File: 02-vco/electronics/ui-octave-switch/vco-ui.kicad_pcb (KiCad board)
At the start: 2 copper layers, 58 x 110 mm, 40 parts, among them J1 Conn_01x04, J2 Conn_02x05_Odd_Even, J3 Conn_02x03_Odd_Even, J4 Conn_01x02, J5 Conn_02x02_Counter_Clockwise, J6 Conn_01x06, U1 0203

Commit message: Designed v0.2 VCO UI (with octave switch)
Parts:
- removed the G*** at (169.3, 149.5)
- removed the G*** at (146.5, 129.6)
- removed the G*** at (163.6, 126.2)
- removed the G*** at (169.0, 63.4)
- removed the G*** at (173.5, 55.2)
- removed JP2, JP3: Jumper_2_Open, Connector_PinHeader_2.54mm:PinHeader_1x02_P2.54mm_Horizontal
- removed RV_FINE1, RV_TUNE1: 100k, Shmoergh_Custom_Footprints:Potentiometer_Bourns_Single-PTV09A
- added C1: C, Capacitor_THT:C_Disc_D5.0mm_W2.5mm_P2.50mm, F.Cu at (162.6, 46.0)
- added C2: C, Capacitor_THT:C_Disc_D5.0mm_W2.5mm_P2.50mm, F.Cu at (179.4, 53.7)
- added G***: LOGO, Shmoergh_Logo:Gyeszno, F.Cu at (177.5, 74.1)
- added G***: LOGO, Shmoergh_Logo:Gyeszno, B.Cu at (159.6, 103.3)
- added G***: LOGO, Shmoergh_Logo:Gyeszno, B.Cu at (144.6, 133.5)
- added R10: 2k, Shmoergh_Custom_Footprints:R_Axial_DIN0207_L6.3mm_D2.5mm_P7.62mm_Horizontal, F.Cu at (160.1, 56.7)
- added R11: 10k (0.1%), Shmoergh_Custom_Footprints:R_Axial_DIN0207_L6.3mm_D2.5mm_P7.62mm_Horizontal, F.Cu at (148.6, 67.0)
- added R12: 10k (0.1%), Shmoergh_Custom_Footprints:R_Axial_DIN0207_L6.3mm_D2.5mm_P7.62mm_Horizontal, F.Cu at (151.8, 74.6)
- added R13: 10k (0.1%), Shmoergh_Custom_Footprints:R_Axial_DIN0207_L6.3mm_D2.5mm_P7.62mm_Horizontal, F.Cu at (155.0, 74.6)
- added R14: 10k (0.1%), Shmoergh_Custom_Footprints:R_Axial_DIN0207_L6.3mm_D2.5mm_P7.62mm_Horizontal, F.Cu at (158.2, 74.6)
- added R15: 10k (0.1%), Shmoergh_Custom_Footprints:R_Axial_DIN0207_L6.3mm_D2.5mm_P7.62mm_Horizontal, F.Cu at (161.3, 74.6)
- added R9: 220k, Shmoergh_Custom_Footprints:R_Axial_DIN0207_L6.3mm_D2.5mm_P7.62mm_Horizontal, F.Cu at (175.7, 119.9)
- added RV_FINE_TUNE1: 100k, Shmoergh_Custom_Footprints:Potentiometer_Bourns_Single-PTV09A, F.Cu at (153.0, 83.0)
- added RV_MAIN_VCO_5V1: 10k, Potentiometer_THT:Potentiometer_Bourns_3006P_Horizontal, F.Cu at (153.8, 62.2)
- added TP_5V1: TP 5V, TestPoint:TestPoint_THTPad_2.0x2.0mm_Drill1.0mm, F.Cu at (145.2, 67.0)
- added U2: TL072, Package_DIP:DIP-8_W7.62mm_LongPads, F.Cu at (165.9, 53.7)
- added U3: 0203, Shmoergh_Custom_Footprints:SR1712-0203, F.Cu at (141.0, 55.0)
- added U_5VREF1: LM336Z5, Package_TO_SOT_THT:TO-92L_Inline_Wide, F.Cu at (159.8, 48.8)
- R1: value 130k -> 100k
- R2, R3: value 100k -> 10k-1M
- R4, R5: value 510k -> 100k
- R7: value 220k -> 100k
- U1: value 0203 -> 0204; footprint Shmoergh_Custom_Footprints:SR1712-0203 -> Shmoergh_Custom_Footprints:SR1712-0204
- moved G*** 76.1 mm to (130.0, 125.8)
- moved J4 72.7 mm to (126.7, 53.2)
- moved G*** 61.9 mm to (168.6, 70.3), turned to 0 degrees
- moved R3 52.8 mm to (178.6, 56.8), turned to -90 degrees
- moved R2 43.3 mm to (175.4, 56.8), turned to -90 degrees
- moved R6 40.8 mm to (169.1, 56.8), turned to -90 degrees
- moved R5 32.1 mm to (172.3, 64.4), turned to 90 degrees
- moved R8 30.2 mm to (175.7, 102.2), turned to -90 degrees
- moved R4 29.7 mm to (128.1, 95.7), turned to 0 degrees
- moved U1 28.3 mm to (137.0, 83.0), turned to 0 degrees
- moved G*** 23.8 mm to (137.0, 83.0)
- moved R7 19.9 mm to (165.9, 56.8), turned to -90 degrees
- moved R1 11.4 mm to (130.1, 111.1), turned to 90 degrees
- moved JP1 0.26 mm to (170.9, 123.8)
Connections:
- JP1 pad 1: NOISE -> SUB
- JP1 pad 3: SUB -> NOISE
- R1 pad 1: +12V -> Net-(J_CV1-PadT)
- R1 pad 2: Net-(R1-Pad2) -> CV
- R2 pad 1: Net-(R2-Pad1) -> Net-(U2A-+)
- R2 pad 2: CV -> PREC_1V
- R3 pad 1: Net-(J_CV1-PadT) -> GND
- R3 pad 2: CV -> Net-(U2A-+)
- R4 pad 1: +12V -> CV
- R5 pad 1: Net-(R5-Pad1) -> PREC_1V
- R5 pad 2: -12V -> Net-(U2A--)
- R6 pad 1: Net-(R6-Pad1) -> Net-(U2A--)
- R6 pad 2: CV -> Net-(R6-Pad2)
- R7 pad 1: Net-(R7-Pad1) -> Net-(R6-Pad2)
- R7 pad 2: SQR_SHAPE -> CV
- R8 pad 1: Net-(J_PWM1-PadT) -> Net-(R8-Pad1)
- RV_PWM1 pad 2: Net-(R7-Pad1) -> Net-(R8-Pad1)
- U1 pad 1: Net-(J_OUT1-PadT) -> Net-(R4-Pad2)
- U1 pad 2: TRI -> GND
- U1 pad 3: SAW -> PREC_1V
- U1 pad 4: SQR -> PREC_2V
- U1 pad 5: unconnected-(U1-Pad5) -> PREC_3V
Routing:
- net -12V: track 24.2 -> 102.5 mm
- net PREC_1V: track 0.00 -> 73.9 mm, vias 0 -> 2
- net Net-(U2A-+): track 0.00 -> 64.1 mm, vias 0 -> 2
- net TRI: track 126.0 -> 69.0 mm
- net Net-(J_PWM1-PadT): track 52.7 -> 6.70 mm
- net CV: track 39.7 -> 85.4 mm, vias 0 -> 4
- net PREC_2V: track 0.00 -> 44.2 mm
- net SAW: track 126.0 -> 170.1 mm, vias 0 -> 2
- net +5V: track 0.00 -> 43.8 mm
- net PREC_3V: track 0.00 -> 42.7 mm
- net Net-(J_CV1-PadT): track 78.5 -> 37.4 mm
- net Net-(R8-Pad1): track 0.00 -> 37.6 mm
- net SYNC_DEFAULT: track 46.3 -> 82.8 mm
- net Net-(R6-Pad1): track 35.2 -> 0.00 mm, vias 2 -> 0
- net Net-(R1-Pad2): track 30.9 -> 0.00 mm, vias 2 -> 0
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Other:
- board text added: "+5V"
- board text added: "HM-02 VCO UI V0.2 2025 SEPT"
- board text added: "OCTAVE"
- board text removed: "CV DEFAULT TO GROUND"
- board text removed: "FM DEFAULT TO GROUND"
- board text removed: "HM-02 VCO UI V0.1 2025 JULY"
- board text removed: "TUNE"

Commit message: Added VCO output to default connector
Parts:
- J6: value Conn_01x06 -> Conn_01x07; footprint Connector_PinSocket_2.54mm:PinSocket_1x06_P2.54mm_Vertical -> Connector_PinSocket_2.54mm:PinSocket_1x07_P2.54mm_Vertical
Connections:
- J6 pad 6: OUT_DEFAULT -> OUT_OUT
- J_OUT1 pad T: Net-(J_OUT1-PadT) -> OUT_OUT
- U3 pad 1: Net-(J_OUT1-PadT) -> OUT_OUT
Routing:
- net OUT_OUT: track 0.00 -> 149.6 mm
- net Net-(J_OUT1-PadT): track 147.0 -> 0.00 mm
- net OUT_DEFAULT: track 38.3 -> 36.0 mm
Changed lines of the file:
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@@
 	(net 19 "EXTRA_DEFAULT")
 	(net 20 "OUT_DEFAULT")
-	(net 21 "Net-(J_OUT1-PadT)")
+	(net 21 "OUT_OUT")
 	(net 22 "Net-(J_PWM1-PadT)")
 	(net 23 "Net-(R4-Pad2)")
@@
 			(layers "*.Cu" "*.Mask")
 			(remove_unused_layers no)
-			(net 21 "Net-(J_OUT1-PadT)")
+			(net 21 "OUT_OUT")
 			(pintype "bidirectional")
 		)
@@
 			(layers "*.Cu" "*.Mask")
 			(remove_unused_layers no)
-			(net 21 "Net-(J_OUT1-PadT)")
+			(net 21 "OUT_OUT")
 			(pinfunction "1")
 			(pintype "output")
@@
 		)
 	)
-	(footprint "Connector_PinSocket_2.54mm:PinSocket_1x06_P2.54mm_Vertical"
+	(footprint "Connector_PinSocket_2.54mm:PinSocket_1x07_P2.54mm_Vertical"
 		(locked yes)
 		(layer "B.Cu")
 		(at 132.5 151 -90)
-		(descr "Through hole straight socket strip, 1x06, 2.54mm pitch, single row (from Kicad 4.0.7), script generated")
-		(tags "Through hole socket strip THT 1x06 2.54mm single row")
+		(descr "Through hole straight socket strip, 1x07, 2.54mm pitch, single row (from Kicad 4.0.7), script generated")
+		(tags "Through hole socket strip THT 1x07 2.54mm single row")
 		(property "Reference" "J6"
-			(at -1.966 -15.122 0)
-			(layer "B.SilkS")
+			(at 0 2.77 90)
+			(layer "User.1")
 			(effects
 				(font
@@
 			)
 		)
-		(property "Value" "Conn_01x06"
-			(at 0 -15.47 90)
+		(property "Value" "Conn_01x07"
+			(at 0 -18.01 90)
 			(layer "B.Fab")
 			(effects
@@
 			)
 		)
-		(property "Description" "Generic connector, single row, 01x06, script generated (kicad-library-utils/schlib/autogen/connector/)"
+		(property "Description" "Generic connector, single row, 01x07, script generated (kicad-library-utils/schlib/autogen/connector/)"
 			(at 0 0 90)
 			(layer "B.Fab")
@@
 		)
 		(property "Part URL" "https://mou.sr/4lnf48h"
-			(at 0 0 90)
+			(at 0 0 270)
 			(unlocked yes)
 			(layer "B.Fab")
@@
 		)
 		(property "Vendor" "Mouser"
-			(at 0 0 90)
+			(at 0 0 270)
 			(unlocked yes)
 			(layer "B.Fab")
@@
 		)
 		(property "LCSC" ""
-			(at 0 0 90)
+			(at 0 0 270)
 			(unlocked yes)
 			(layer "B.Fab")
@@
 			)
 		)
+		(property "Part No." ""
+			(at 0 0 270)
+			(unlocked yes)
+			(layer "B.Fab")
+			(hide yes)
+			(effects
+				(font
+					(size 1 1)
+					(thickness 0.15)
+				)
+				(justify mirror)
+			)
+		)
 		(property ki_fp_filters "Connector*:*_1x??_*")
 		(sheetname "/")
@@
 		(fp_line
 			(start -1.33 -1.27)
-			(end -1.33 -14.03)
+			(end -1.33 -16.57)
 			(stroke
 				(width 0.12)
@@
 		(fp_line
 			(start 1.33 -1.27)
-			(end 1.33 -14.03)
+			(end 1.33 -16.57)
 			(stroke
 				(width 0.12)
@@
 		)
 		(fp_line
-			(start -1.33 -14.03)
-			(end 1.33 -14.03)
+			(start -1.33 -16.57)
+			(end 1.33 -16.57)
 			(stroke
 				(width 0.12)
@@
 		(fp_line
 			(start 1.75 1.8)
-			(end 1.75 -14.45)
+			(end 1.75 -17)
 			(stroke
 				(width 0.05)
@@
 		)
 		(fp_line
-			(start -1.8 -14.45)
+			(start -1.8 -17)
 			(end -1.8 1.8)
 			(stroke
@@
 		)
 		(fp_line
-			(start 1.75 -14.45)
-			(end -1.8 -14.45)
+			(start 1.75 -17)
+			(end -1.8 -17)
 			(stroke
 				(width 0.05)
@@
 		(fp_line
 			(start 1.27 0.635)
-			(end 1.27 -13.97)
+			(end 1.27 -16.51)
 			(stroke
 				(width 0.1)
@@
 		)
 		(fp_line
-			(start -1.27 -13.97)
+			(start -1.27 -16.51)
 			(end -1.27 1.27)
 			(stroke
@@
 		)
 		(fp_line
-			(start 1.27 -13.97)
-			(end -1.27 -13.97)
+			(start 1.27 -16.51)
+			(end -1.27 -16.51)
 			(stroke
 				(width 0.1)
@@
 		)
 		(fp_text user "${REFERENCE}"
-			(at 0 -6.35 180)
+			(at 0 -7.62 0)
 			(layer "B.Fab")
 			(effects
@@
 			(layers "*.Cu" "*.Mask")
 			(remove_unused_layers no)
-			(net 20 "OUT_DEFAULT")
+			(net 21 "OUT_OUT")
 			(pinfunction "Pin_6")
 			(pintype "passive")
 		)
+		(pad "7" thru_hole circle
+			(at 0 -15.24 270)
+			(size 1.7 1.7)
+			(drill 1)
+			(layers "*.Cu" "*.Mask")
+			(remove_unused_layers no)
+			(net 20 "OUT_DEFAULT")
+			(pinfunction "Pin_7")
+			(pintype "passive")
+		)
 		(embedded_fonts no)
-		(model "${KICAD9_3DMODEL_DIR}/Connector_PinSocket_2.54mm.3dshapes/PinSocket_1x06_P2.54mm_Vertical.step"
+		(model "${KICAD9_3DMODEL_DIR}/Connector_PinSocket_2.54mm.3dshapes/PinSocket_1x07_P2.54mm_Vertical.step"
 			(offset
 				(xyz 0 0 0)
@@
 		)
 	)
+	(gr_text "OUT"
+		(at 147.876 149.029 0)
+		(layer "F.SilkS")
+		(effects
+			(font
+				(size 1 0.75)
+				(thickness 0.17)
+				(bold yes)
+			)
+			(justify bottom)
+		)
+	)
 	(gr_text "NOISE"
 		(at 181.023 136.964 90)
@@
 	(segment
 		(start 162.862 150.553)
-		(end 161.211 152.204)
+		(end 160.957 152.458)
 		(width 0.508)
 		(layer "F.Cu")
@@
 	)
 	(segment
-		(start 161.211 152.204)
-		(end 146.404 152.204)
+		(start 160.957 152.458)
+		(end 149.198 152.458)
 		(width 0.508)
 		(layer "F.Cu")
@@
 	)
 	(segment
-		(start 146.404 152.204)
-		(end 145.2 151)
+		(start 149.198 152.458)
+		(end 147.74 151)
 		(width 0.508)
 		(layer "F.Cu")
@@
 	)
 	(segment
-		(start 125.143 141.155)
-		(end 130.731 146.743)
+		(start 125.143 61.272)
+		(end 125.143 141.155)
 		(width 0.508)
 		(layer "F.Cu")
@@
 	)
 	(segment
-		(start 130.731 152.077)
-		(end 131.747 153.093)
+		(start 166.672 153.347)
+		(end 169 151.019)
 		(width 0.508)
 		(layer "F.Cu")
@@
 	)
 	(segment
-		(start 131.85 60)
-		(end 126.415 60)
+		(start 147.749 153.347)
+		(end 166.672 153.347)
 		(width 0.508)
 		(layer "F.Cu")
@@
 	)
 	(segment
+		(start 145.2 153.338)
+		(end 145.209 153.347)
+		(width 0.508)
+		(layer "F.Cu")
+		(net 21)
+	)
+	(segment
+		(start 145.209 153.347)
+		(end 147.749 153.347)
+		(width 0.508)
+		(layer "F.Cu")
+		(net 21)
+	)
+	(segment
 		(start 130.731 146.743)
 		(end 130.731 152.077)
@@
 	)
 	(segment
-		(start 125.143 61.272)
-		(end 125.143 141.155)
+		(start 130.731 152.077)
+		(end 132.001 153.347)
 		(width 0.508)
 		(layer "F.Cu")
@@
 	)
 	(segment
-		(start 131.747 153.093)
-		(end 166.926 153.093)
+		(start 132.001 153.347)
+		(end 145.209 153.347)
 		(width 0.508)
 		(layer "F.Cu")
@@
 	)
 	(segment
-		(start 166.926 153.093)
-		(end 169 151.019)
+		(start 131.85 60)
+		(end 126.415 60)
+		(width 0.508)
+		(layer "F.Cu")
+		(net 21)
+	)
+	(segment
+		(start 125.143 141.155)
+		(end 130.731 146.743)
 		(width 0.508)
 		(layer "F.Cu")
@@
 		(width 0.508)
 		(layer "F.Cu")
+		(net 21)
+	)
+	(segment
+		(start 145.2 151)
+		(end 145.2 153.338)
+		(width 0.508)
+		(layer "F.Cu")

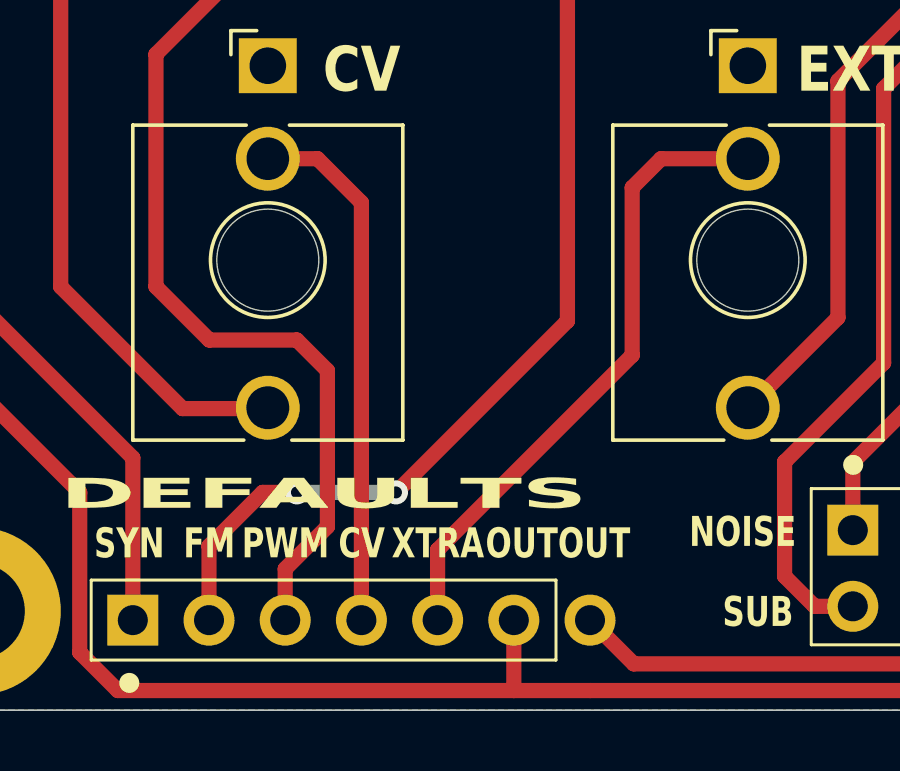
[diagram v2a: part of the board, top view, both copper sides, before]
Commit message: Added CV output to VCO default patch
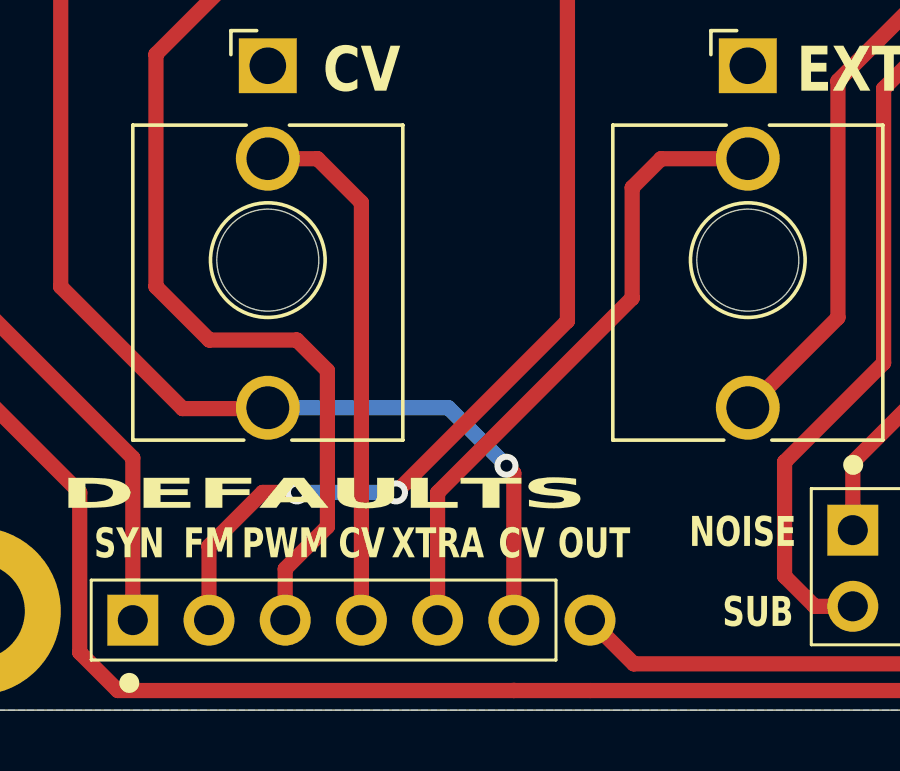
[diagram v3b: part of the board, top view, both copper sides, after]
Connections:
- J6 pad 6: OUT_OUT -> CV_INPUT
- J_CV1 pad T: Net-(J_CV1-PadT) -> CV_INPUT
- J_OUT1 pad T: OUT_OUT -> Net-(J_OUT1-PadT)
- R1 pad 1: Net-(J_CV1-PadT) -> CV_INPUT
- U3 pad 1: OUT_OUT -> Net-(J_OUT1-PadT)
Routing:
- net OUT_OUT: track 149.6 -> 0.00 mm
- net Net-(J_OUT1-PadT): track 0.00 -> 147.2 mm
- net CV_INPUT: track 0.00 -> 51.4 mm, vias 0 -> 1
- net Net-(J_CV1-PadT): track 37.4 -> 0.00 mm
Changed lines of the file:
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@@
 	(net 16 "SUB")
 	(net 17 "Net-(JP1-C)")
-	(net 18 "Net-(J_CV1-PadT)")
+	(net 18 "CV_INPUT")
 	(net 19 "EXTRA_DEFAULT")
 	(net 20 "OUT_DEFAULT")
-	(net 21 "OUT_OUT")
+	(net 21 "Net-(J_OUT1-PadT)")
 	(net 22 "Net-(J_PWM1-PadT)")
 	(net 23 "Net-(R4-Pad2)")
@@
 			(layers "*.Cu" "*.Mask")
 			(remove_unused_layers no)
-			(net 21 "OUT_OUT")
+			(net 21 "Net-(J_OUT1-PadT)")
 			(pintype "bidirectional")
 		)
@@
 			(layers "*.Cu" "*.Mask")
 			(remove_unused_layers no)
-			(net 18 "Net-(J_CV1-PadT)")
+			(net 18 "CV_INPUT")
 			(pintype "bidirectional")
 		)
@@
 			(layers "*.Cu" "*.Mask")
 			(remove_unused_layers no)
-			(net 18 "Net-(J_CV1-PadT)")
+			(net 18 "CV_INPUT")
 			(pintype "passive")
 		)
@@
 			(layers "*.Cu" "*.Mask")
 			(remove_unused_layers no)
-			(net 21 "OUT_OUT")
+			(net 21 "Net-(J_OUT1-PadT)")
 			(pinfunction "1")
 			(pintype "output")
@@
 			(layers "*.Cu" "*.Mask")
 			(remove_unused_layers no)
-			(net 21 "OUT_OUT")
+			(net 18 "CV_INPUT")
 			(pinfunction "Pin_6")
 			(pintype "passive")
@@
 		)
 	)
-	(gr_text "OUT"
+	(gr_text "CV"
 		(at 145.463 149.029 0)
 		(layer "F.SilkS" knockout)
@@
 	)
 	(segment
+		(start 145.2 151)
+		(end 145.2 146.099)
+		(width 0.508)
+		(layer "F.Cu")
+		(net 18)
+	)
+	(segment
+		(start 145.2 146.099)
+		(end 144.955 145.854)
+		(width 0.508)
+		(layer "F.Cu")
+		(net 18)
+	)
+	(segment
 		(start 130.096 111.056)
 		(end 130.096 139.885)
@@
 		(net 18)
 	)
+	(via
+		(at 144.955 145.854)
+		(size 0.8)
+		(drill 0.4)
+		(layers "F.Cu" "B.Cu")
+		(net 18)
+	)
 	(segment
-		(start 149.146 142.171)
-		(end 149.146 136.583)
+		(start 144.955 145.854)
+		(end 143.021 143.92)
 		(width 0.508)
-		(layer "F.Cu")
-		(net 19)
+		(layer "B.Cu")
+		(net 18)
+	)
+	(segment
+		(start 143.021 143.92)
+		(end 137 143.92)
+		(width 0.508)
+		(layer "B.Cu")
+		(net 18)
 	)
 	(segment
@@
 	)
 	(segment
-		(start 142.66 148.657)
-		(end 149.146 142.171)
+		(start 142.66 151)
+		(end 142.66 146.752)
 		(width 0.508)
 		(layer "F.Cu")
@@
 	)
 	(segment
-		(start 142.66 151)
-		(end 142.66 148.657)
+		(start 149.146 136.583)
+		(end 150.109 135.62)
 		(width 0.508)
 		(layer "F.Cu")
@@
 	)
 	(segment
-		(start 149.146 136.583)
-		(end 150.109 135.62)
+		(start 142.66 146.752)
+		(end 149.146 140.266)
+		(width 0.508)
+		(layer "F.Cu")
+		(net 19)
+	)
+	(segment
+		(start 149.146 140.266)
+		(end 149.146 136.583)
 		(width 0.508)
 		(layer "F.Cu")
@@
 		(width 0.508)
 		(layer "F.Cu")
-		(net 21)
-	)
-	(segment
-		(start 145.2 151)
-		(end 145.2 153.338)
-		(width 0.508)
-		(layer "F.Cu")
